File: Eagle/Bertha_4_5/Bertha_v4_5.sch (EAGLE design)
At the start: 131 parts, among them CON1 JACK_DC_BARREL, CON2 JACK_DC_BARREL, IC1 MCP1703DB, IC4 DRV8811, J1 RJ12RIGHTANGLE-I2C, J2 RJ12RIGHTANGLE-I2C, Q5 BSP75, Q6 BSP75, U1 HX711, X1 1503_09, X2 8MHz, X3 FH12-08S-1SH, X4 MINI-USB

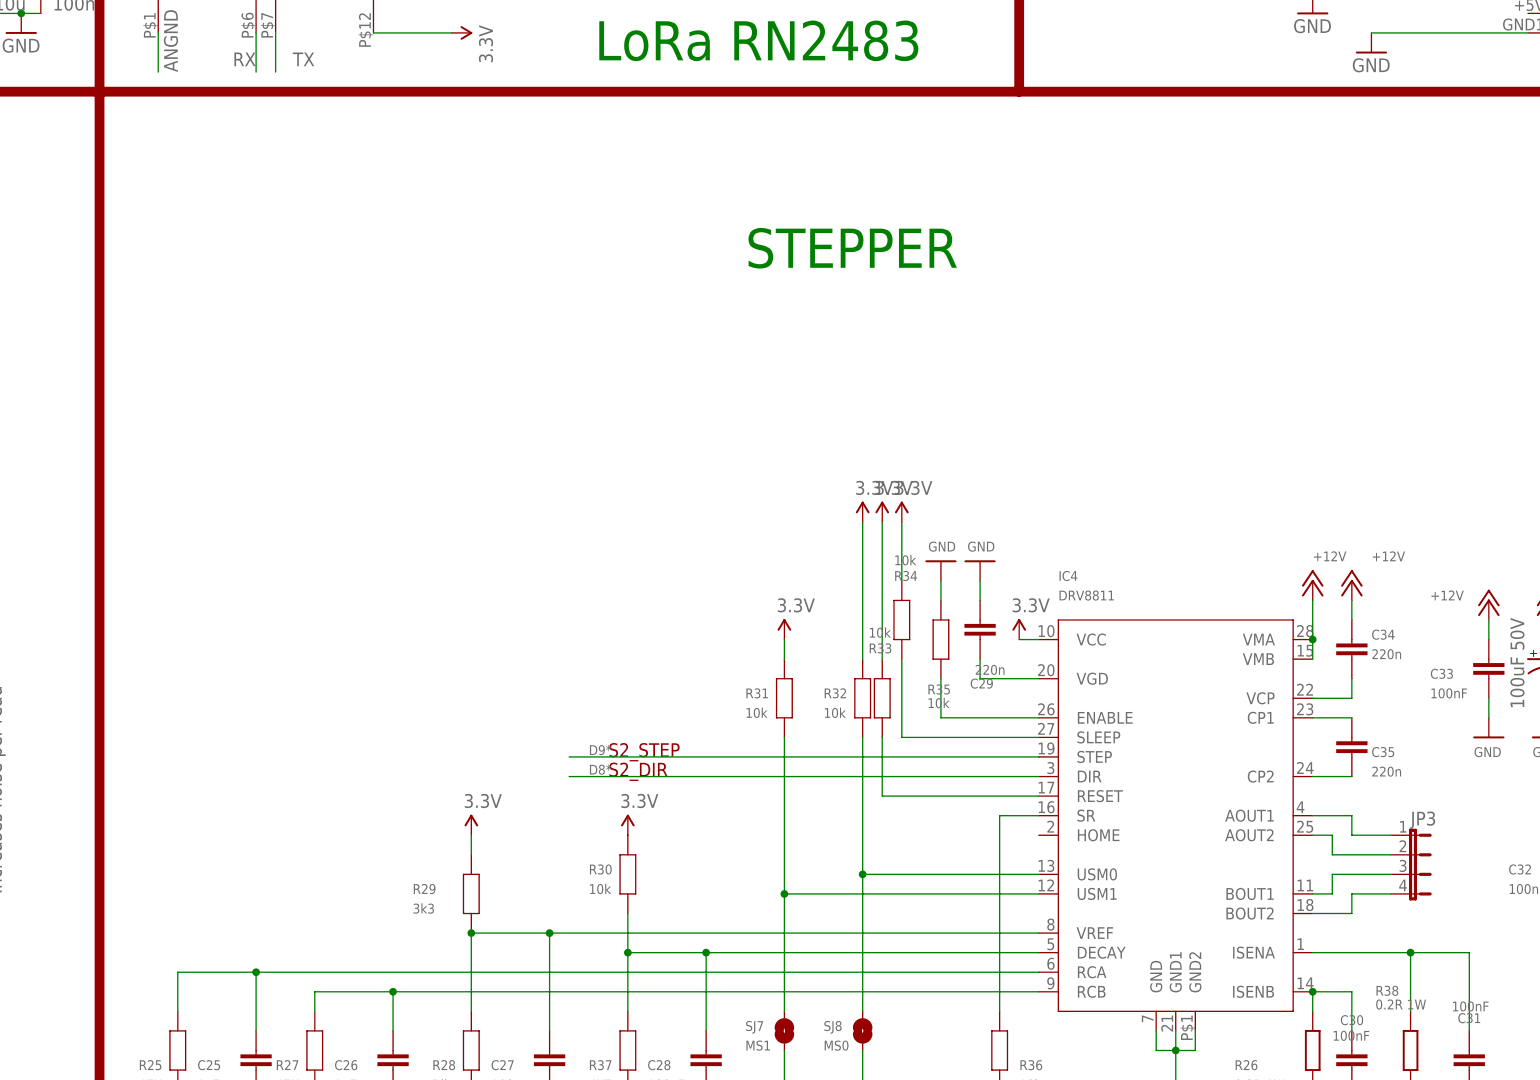
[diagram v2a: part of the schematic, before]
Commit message: Added LEDs for DRV8811 Stepper Driver closes #83
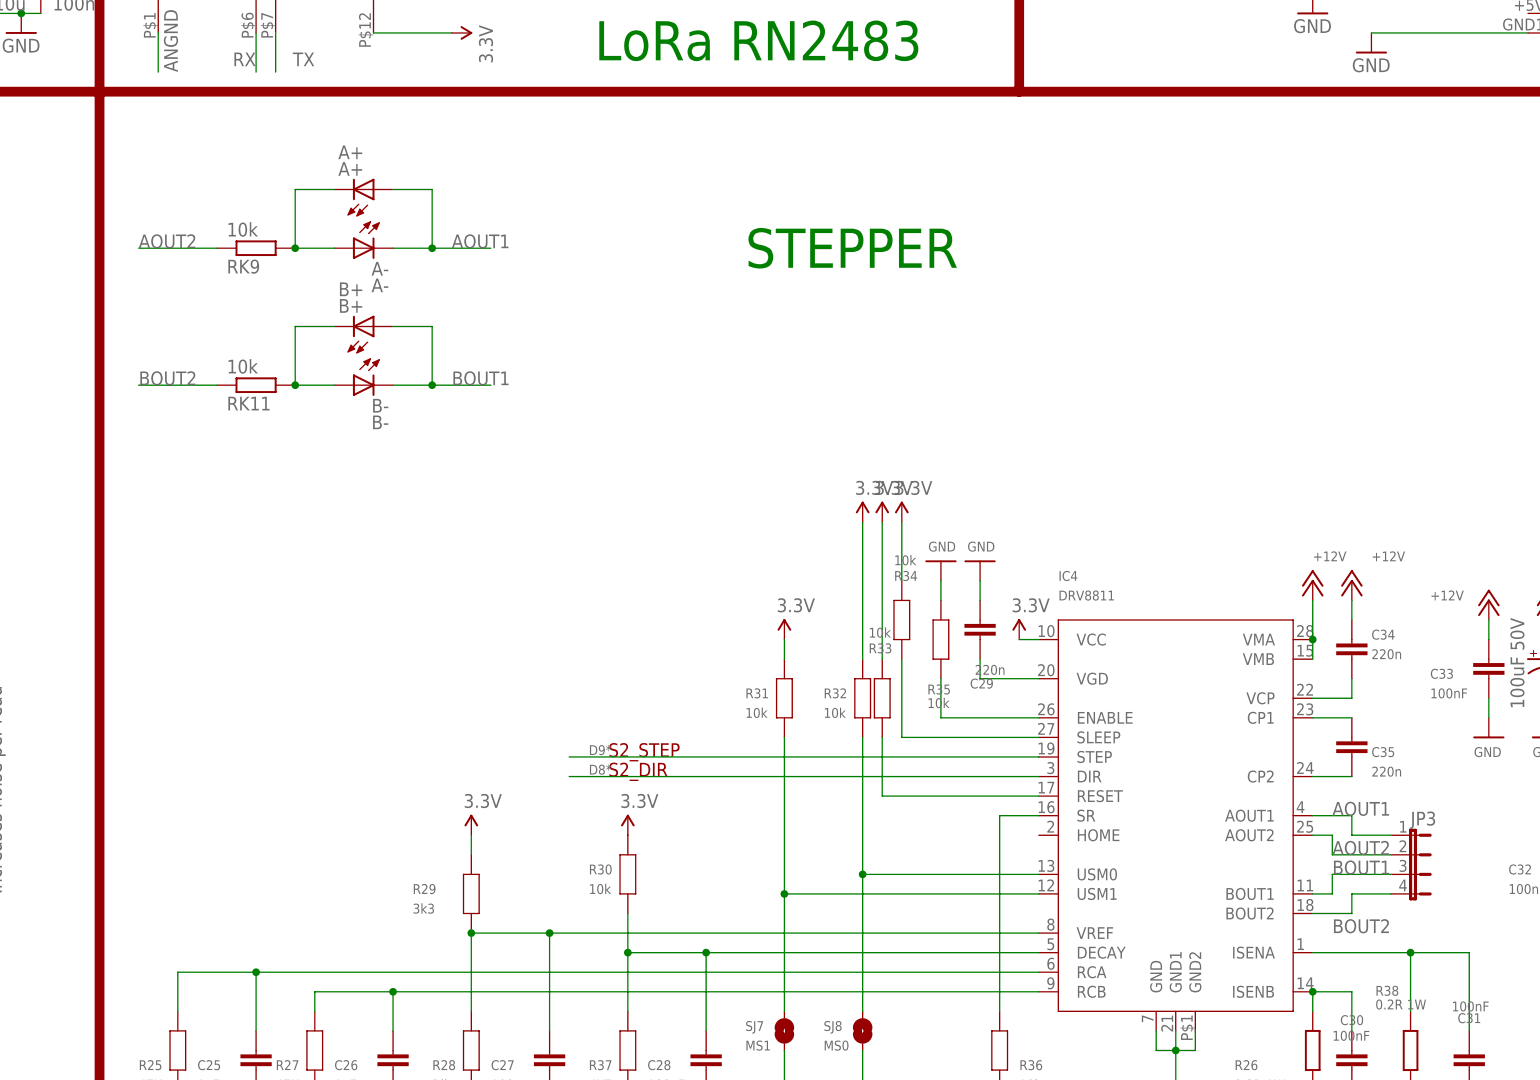
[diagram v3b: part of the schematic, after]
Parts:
- added A+: A+, adafruit:LEDCHIP-LED0805
- added A-: A-, adafruit:LEDCHIP-LED0805
- added B+: B+, adafruit:LEDCHIP-LED0805
- added B-: B-, adafruit:LEDCHIP-LED0805
- added RK11, RK9: 10k, rcl:R-EU_R0805
- C30: device freetronics-master-v1:CAP0603 -> freetronics-master-v1:CAP0805
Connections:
- removed net N$10: IC4.AOUT2, JP3.2
- removed net N$4: IC4.BOUT2, JP3.4
- removed net N$55: IC4.AOUT1, JP3.1
- removed net N$56: IC4.BOUT1, JP3.3
- new net AOUT1: A+.A, A-.C, IC4.AOUT1, JP3.1
- new net AOUT2: IC4.AOUT2, JP3.2, RK9.1
- new net BOUT1: B+.A, B-.C, IC4.BOUT1, JP3.3
- new net BOUT2: IC4.BOUT2, JP3.4, RK11.1
- new net N$15: A+.C, A-.A, RK9.2
- new net N$19: B+.C, B-.A, RK11.2

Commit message: changed the SMA edge connector forrpting fot LoRa antenna. Foortptint to be checked, Gerbers to be Regenerated !
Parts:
- 868MHZ: device sma_end_launch:SMACONNECTOR_EDGE -> sma_end_launch:SMACONNECTOR_EDGE_UFL
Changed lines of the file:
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@@
 <part name="P+42" library="SparkFun" deviceset="3.3V" device=""/>
 <part name="P+43" library="supply1" deviceset="+12V" device=""/>
-<part name="868MHZ" library="sma_end_launch" deviceset="SMACONNECTOR" device="_EDGE"/>
+<part name="868MHZ" library="sma_end_launch" deviceset="SMACONNECTOR" device="_EDGE_UFL"/>
 <part name="D1" library="lpatiny" deviceset="1N581*" device="D1206" value="1N581D1206"/>
 <part name="SUPPLY1" library="supply2" deviceset="VDD" device=""/>
